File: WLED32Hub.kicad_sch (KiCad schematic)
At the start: 55 parts, among them J1 USB_C_Receptacle_PowerOnly_6P, J10 WAGO, J11 WAGO, J12 WAGO, J13 WAGO, J14 WAGO, J15 WAGO, J16 WAGO, J17 WAGO, J18 WAGO, J19 Conn_01x05, J2 Power WAGO, J3 WAGO, J4 WAGO, J5 WAGO, J6 WAGO, J7 WAGO, J8 WAGO, J9 WAGO, Q1 IRLB8721PBF, Q10 IRLB8721PBF, Q11 IRLB8721PBF, Q12 IRLB8721PBF, Q13 IRLB8721PBF, Q14 IRLB8721PBF, Q15 IRLB8721PBF, Q16 IRLB8721PBF, Q2 IRLB8721PBF, Q3 IRLB8721PBF, Q4 IRLB8721PBF, Q5 IRLB8721PBF, Q6 IRLB8721PBF, Q7 IRLB8721PBF, Q8 IRLB8721PBF, Q9 IRLB8721PBF, U1 ESP32-DevKit-V3.0, U2 Arduino-Pro-Micro

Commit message: Connect LED 4
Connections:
- net LED4: now also U1.15 (P13)
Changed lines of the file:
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@@
+	(wire
+		(pts
+			(xy 85.09 58.42) (xy 90.17 58.42)
+		)
+		(stroke
+			(width 0)
+			(type default)
+		)
+	)
 	(wire
 		(pts

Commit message: Create & Assign all Footprints
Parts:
- added TP1, TP2, TP3, TP4: TestPoint, TestPoint:TestPoint_Pad_1.5x1.5mm, symbol Connector:TestPoint
- J10, J11, J12, J13, J14, J15, J16, J17, J18, J3, J4, J5, J6, J7, J8, J9: footprint (none) -> TerminalBlock_WAGO:TerminalBlock_WAGO_2601-1102_1x02_P3.50mm_Horizontal
- J19: footprint (none) -> footprints:SolderWirePad_1x05_SMD_1x2mm
- J2: footprint (none) -> footprints:WAGO_2606-1102
- R1, R10, R11, R12, R13, R14, R15, R16, R17, R18, R2, R3, R4, R5, R6, R7, R8, R9: footprint (none) -> Resistor_THT:R_Axial_DIN0309_L9.0mm_D3.2mm_P12.70mm_Horizontal
- U1: footprint (none) -> footprints:ESP32_DevKit_V3.0
- U2: footprint (none) -> footprints:Arduino_Pro_Micro
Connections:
- net GND: now also TP2.1
- net GND1: now also TP4.1
- net VCC: now also TP1.1
- net VLED: now also TP3.1

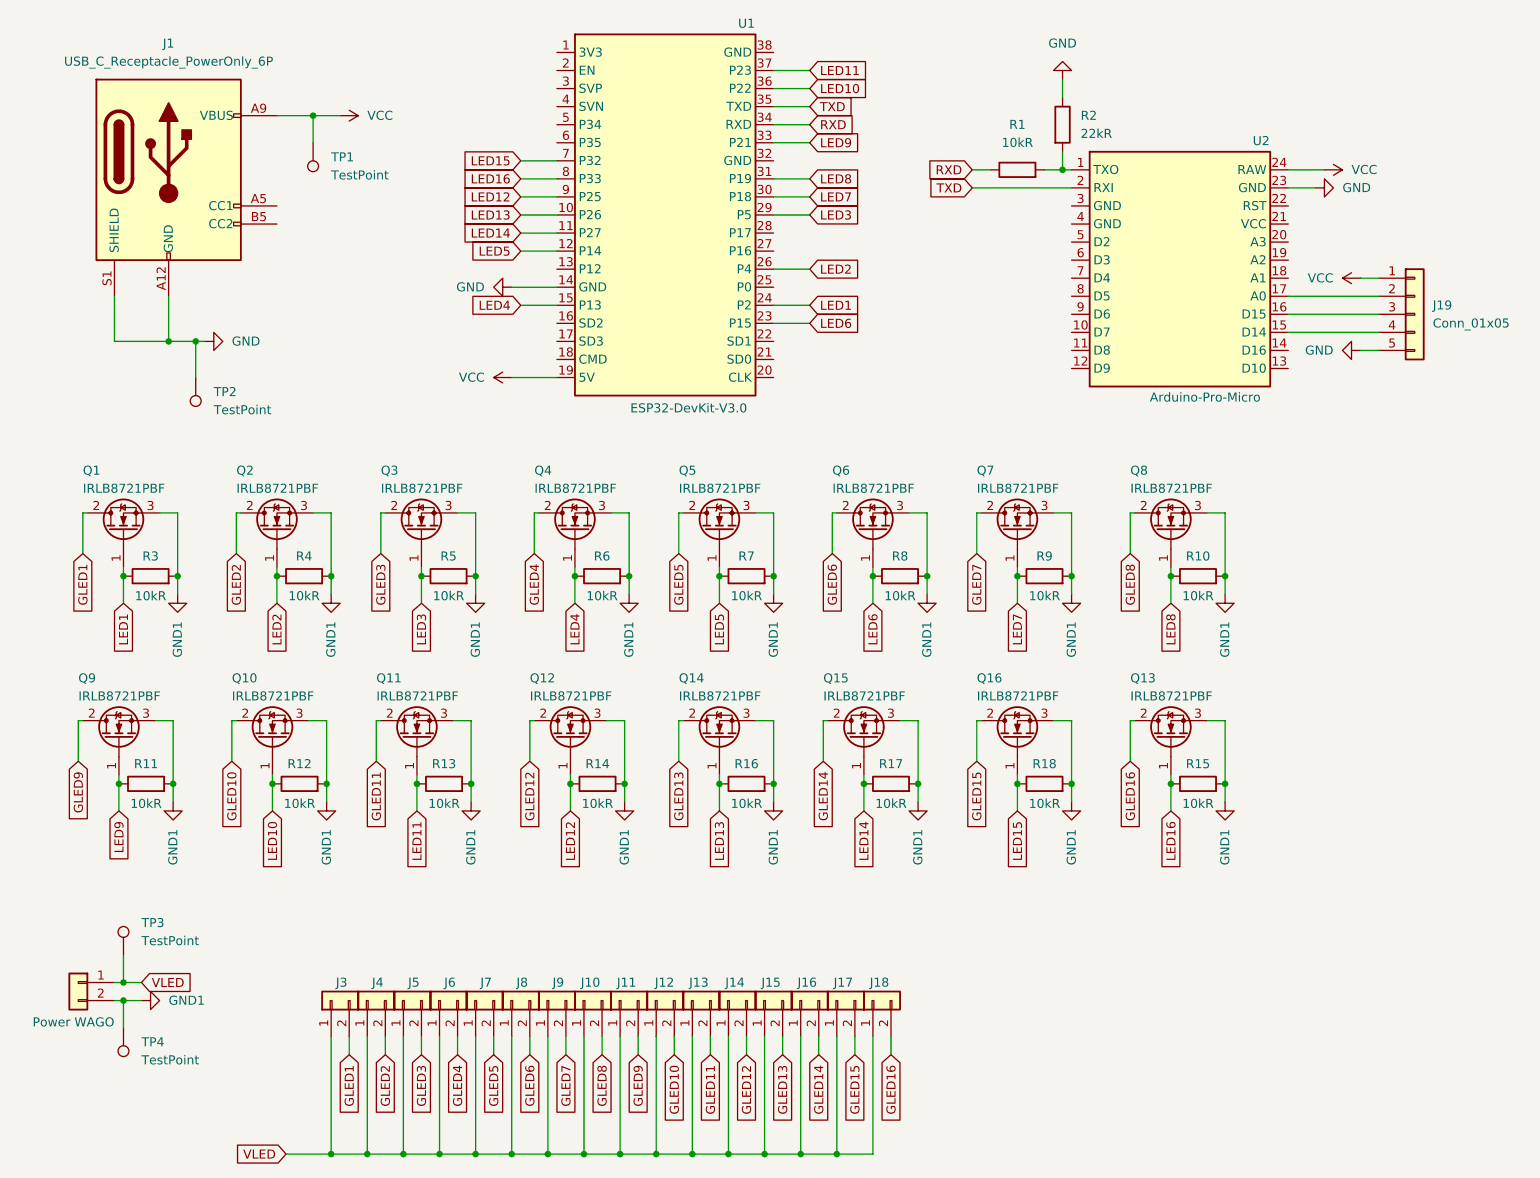
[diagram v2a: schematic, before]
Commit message: Add Components to PCB
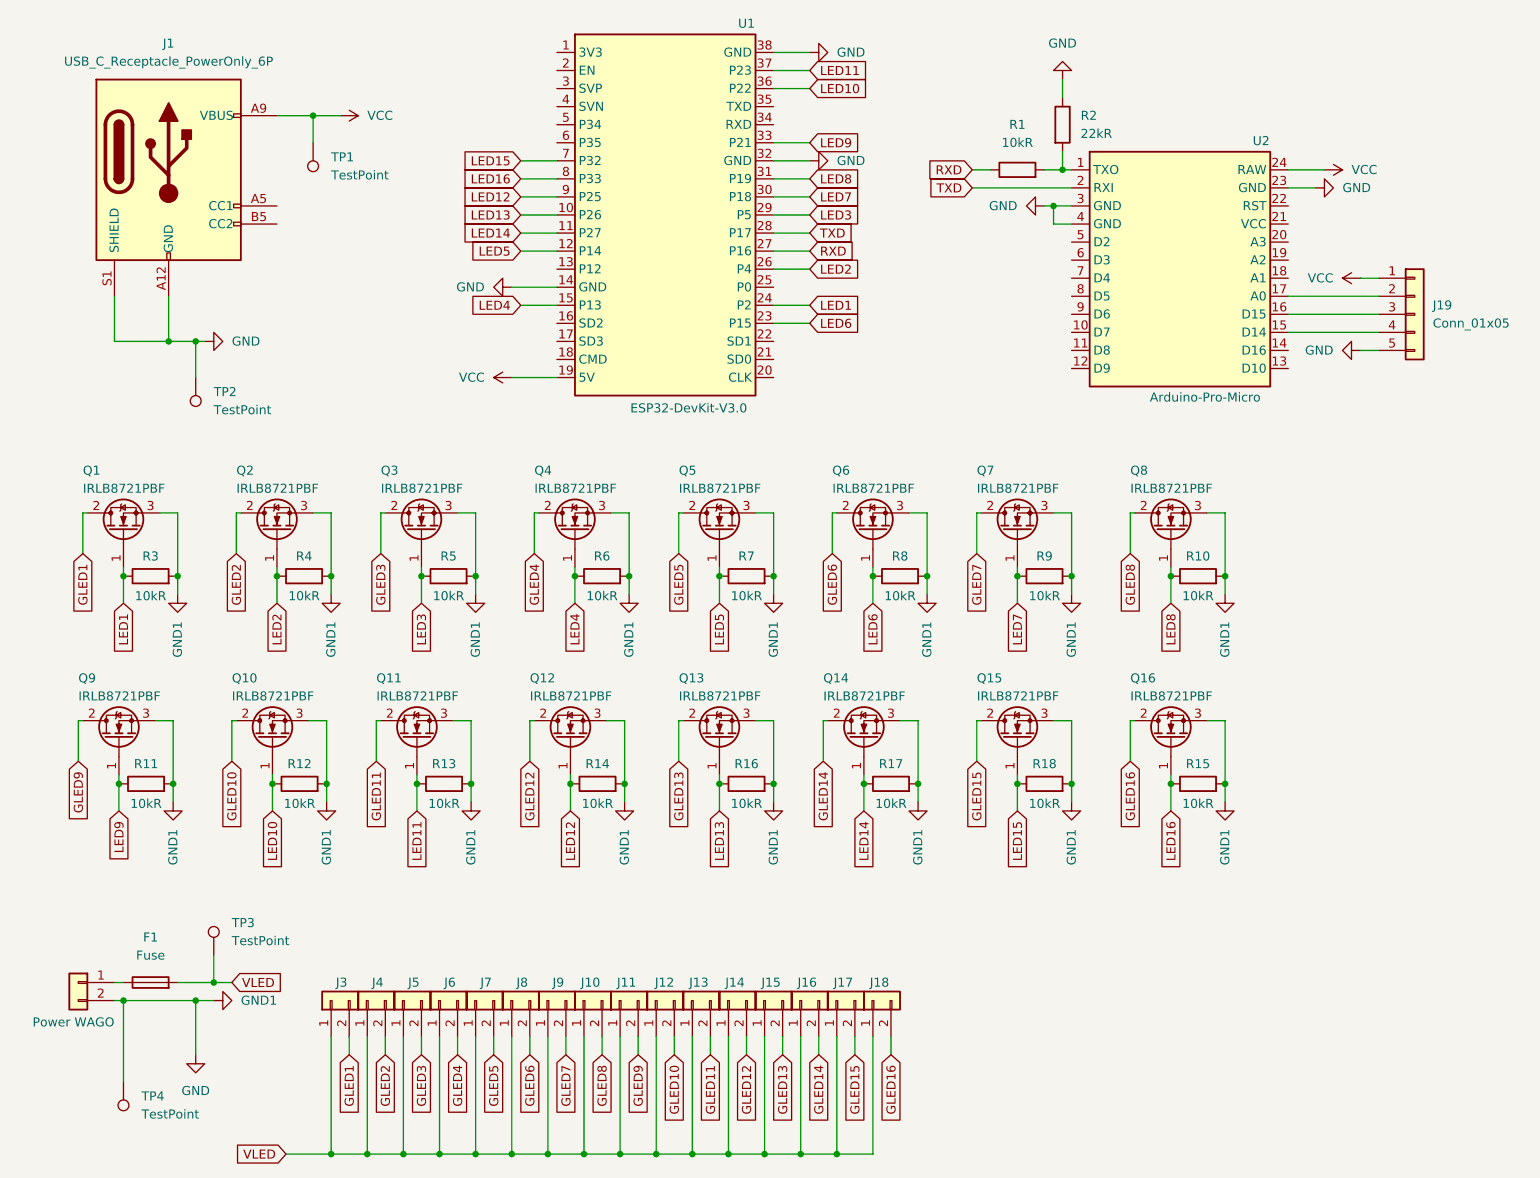
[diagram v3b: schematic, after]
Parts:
- added F1: Fuse, Fuse:Fuseholder_Blade_ATO_Littelfuse_Pudenz_2_Pin, symbol Device:Fuse
- renumbered Q14 to Q13, Q15 to Q14, Q16 to Q15, Q13 to Q16
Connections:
- net GND1 is gone; now on net GND: J2.2 (Pin_2), Q1.3 (S), Q10.3 (S), Q11.3 (S), Q12.3 (S), Q13.3 (S), Q14.3 (S), Q15.3 (S), Q16.3 (S), Q2.3 (S), Q3.3 (S), Q4.3 (S), Q5.3 (S), Q6.3 (S), Q7.3 (S), Q8.3 (S), Q9.3 (S), R10.2, R11.2, R12.2, R13.2, R14.2, R15.2, R16.2, R17.2, R18.2, R3.2, R4.2, R5.2, R6.2, R7.2, R8.2, R9.2, TP4.1
- net GND: now also U1.32 (GND), U1.38 (GND), U2.3 (GND), U2.4 (GND)
- net RXD: now also U1.27 (P16); no longer U1.34 (RXD)
- net TXD: now also U1.28 (P17); no longer U1.35 (TXD)
- net VLED: now also F1.2; no longer J2.1 (Pin_1)
- new net: F1.1, J2.1 (Pin_1)
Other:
- moved on the sheet: TP3, TP4

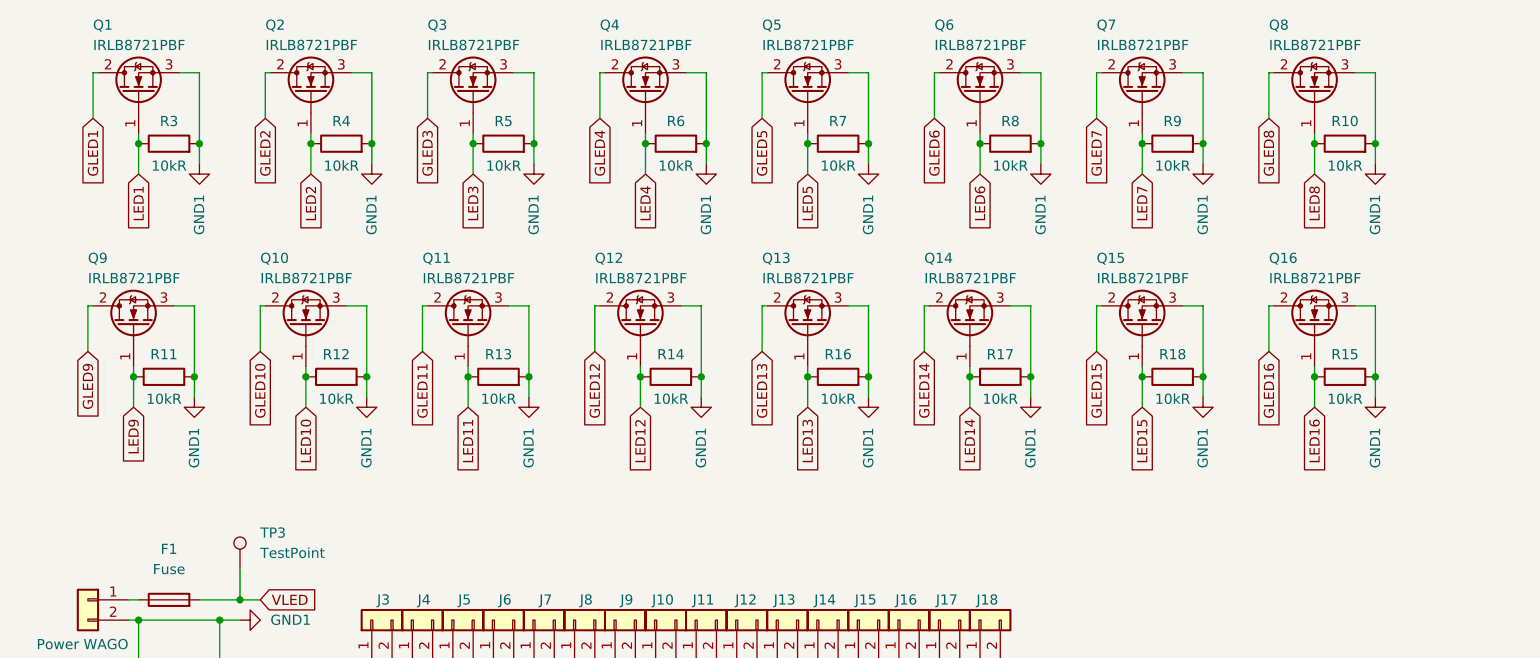
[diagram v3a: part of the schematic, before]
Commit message: Adding Test Points to LED Switching Signals
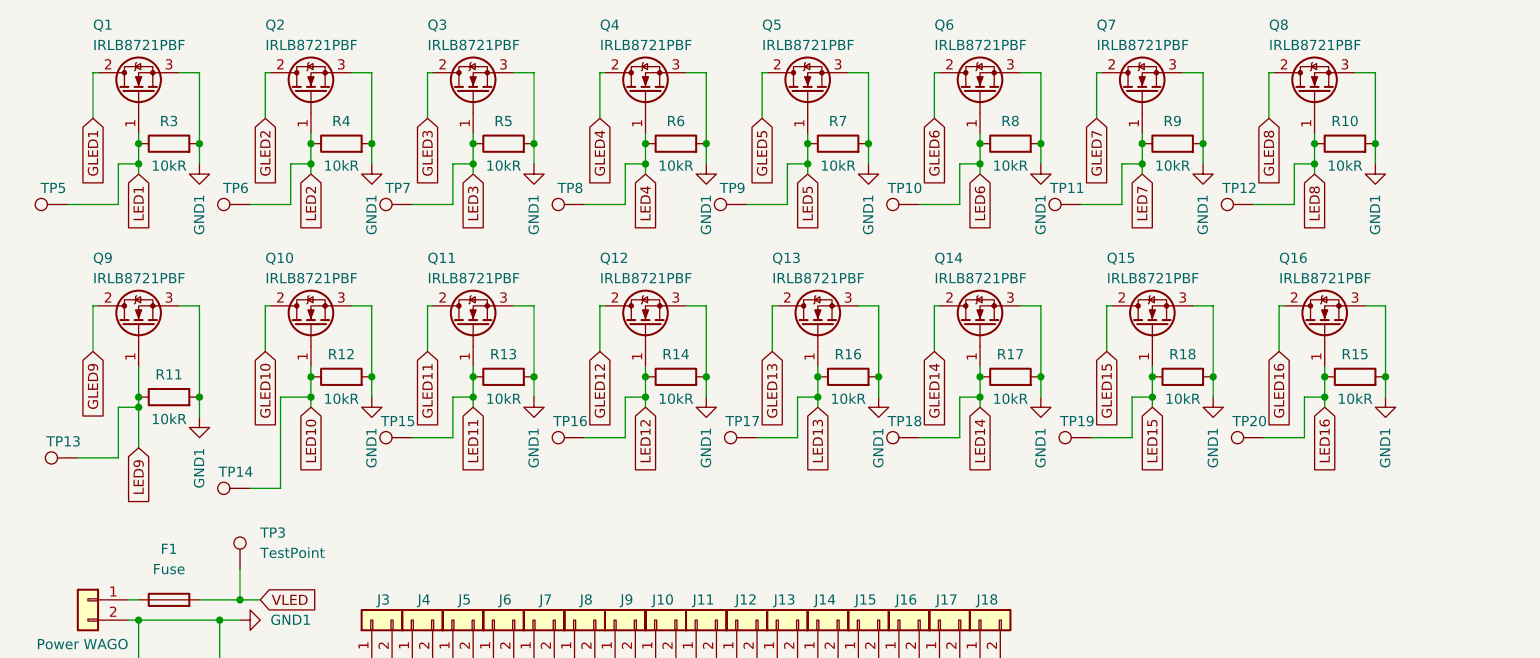
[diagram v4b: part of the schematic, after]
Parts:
- added TP10, TP11, TP12, TP13, TP14, TP15, TP16, TP17, TP18, TP19, TP20, TP5, TP6, TP7, TP8, TP9: TestPoint, TestPoint:TestPoint_Pad_1.5x1.5mm, symbol Connector:TestPoint
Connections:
- net LED1: now also TP5.1
- net LED10: now also TP14.1
- net LED11: now also TP15.1
- net LED12: now also TP16.1
- net LED13: now also TP17.1
- net LED14: now also TP18.1
- net LED15: now also TP19.1
- net LED16: now also TP20.1
- net LED2: now also TP6.1
- net LED3: now also TP7.1
- net LED4: now also TP8.1
- net LED5: now also TP9.1
- net LED6: now also TP10.1
- net LED7: now also TP11.1
- net LED8: now also TP12.1
- net LED9: now also TP13.1
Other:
- moved on the sheet: Q10, Q11, Q12, Q13, Q14, Q15, Q16, Q9, R11, R12, R13, R14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
